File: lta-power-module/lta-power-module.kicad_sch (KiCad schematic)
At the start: 9 parts

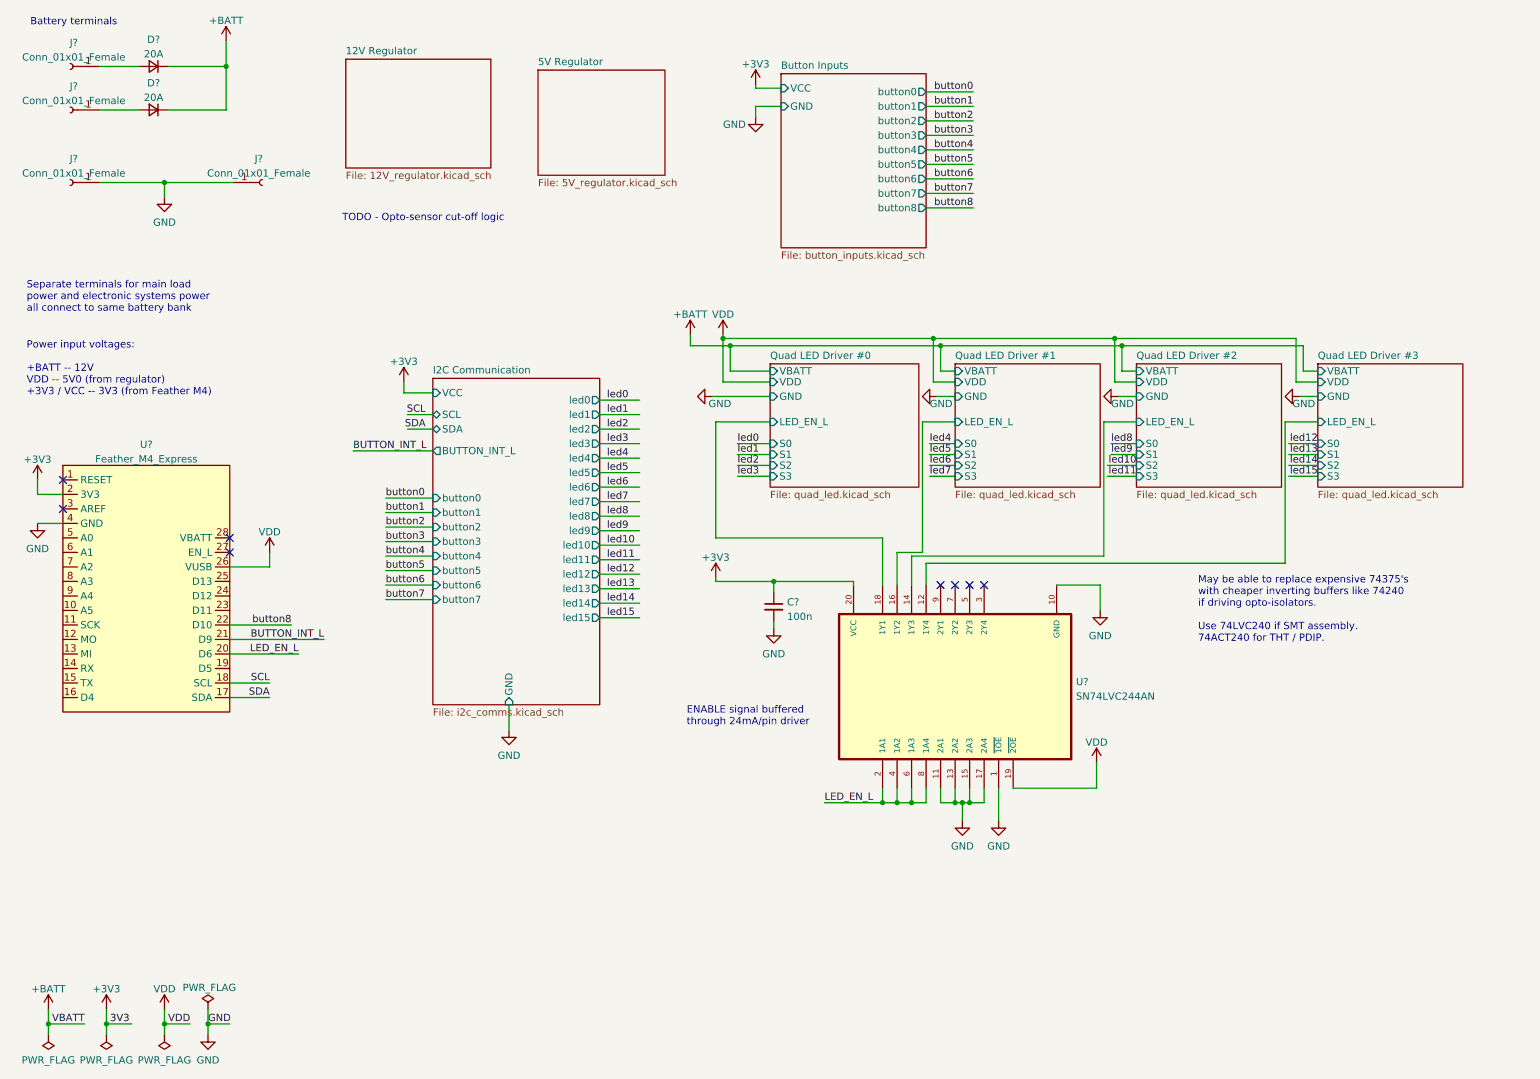
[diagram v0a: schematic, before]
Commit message: Power module main electrical schematic drawn, unannotated.
A logical schematic including flying wire connections between off-board
modules is sketched in the associated pptx file.
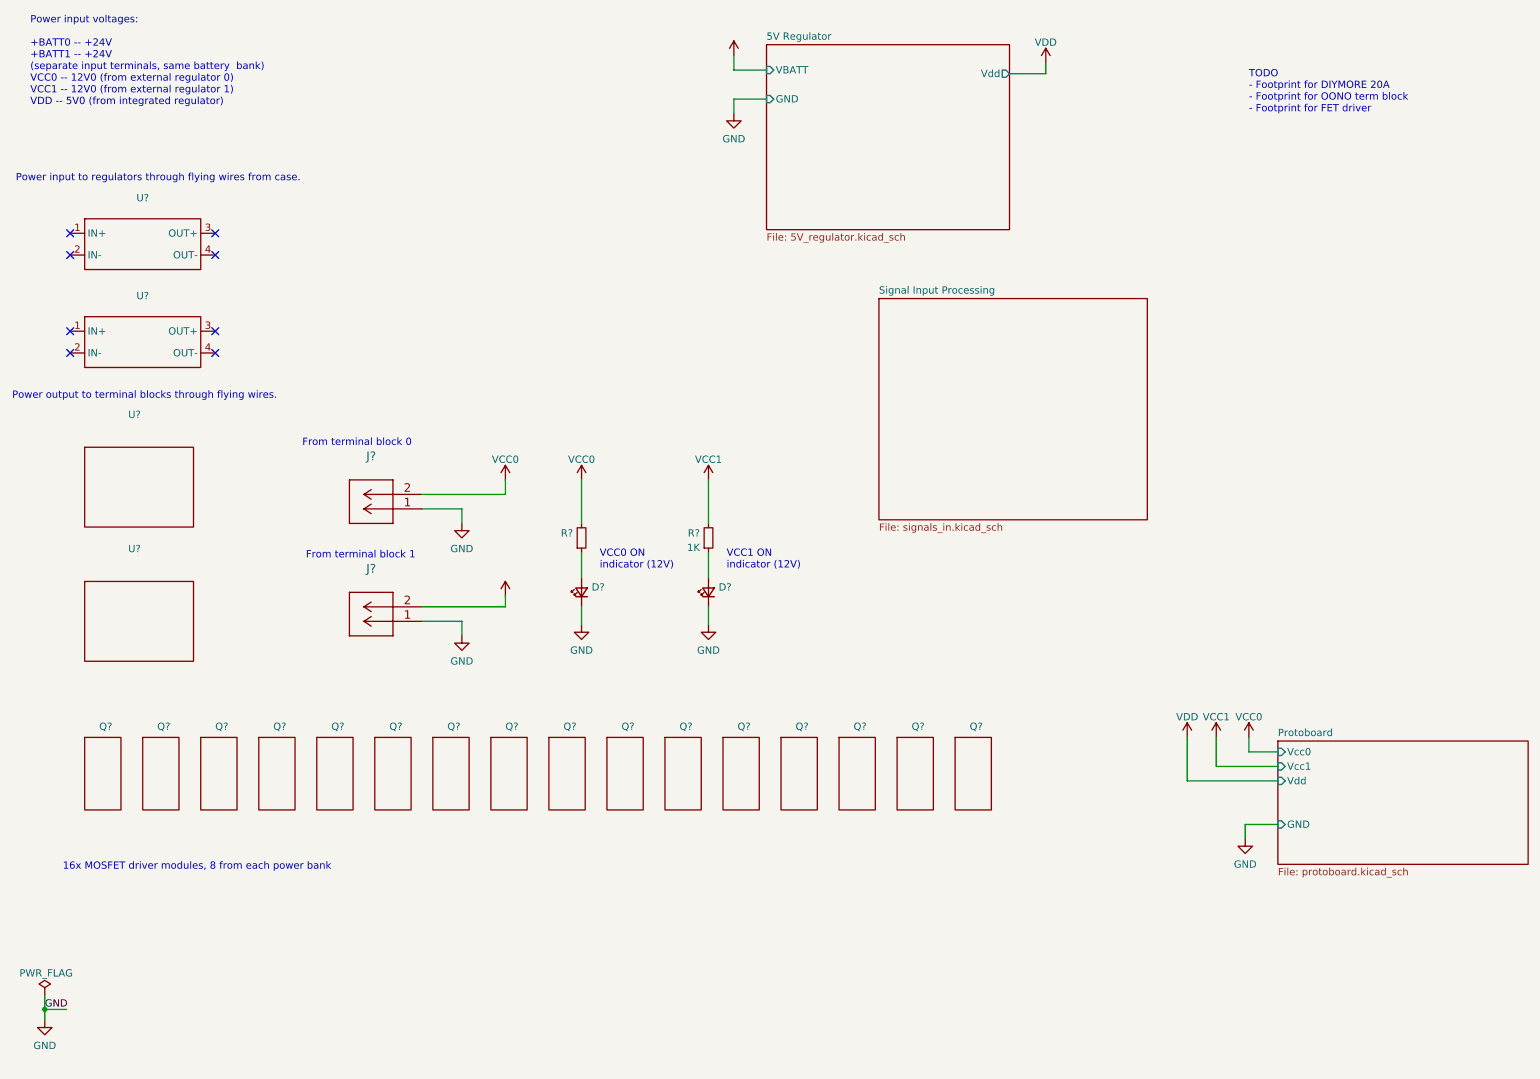
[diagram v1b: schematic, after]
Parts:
- removed C?: 100n, symbol Device:C_Small
- removed D? (x2): 20A, symbol Device:D_Small
- removed J? (x4): Conn_01x01_Female, symbol Connector:Conn_01x01_Female
- removed U?: SN74LVC244AN, Aaron_TI_Parts:TI_N_R-PDIP-T20, symbol Aaron-TI-Buffers:SN74LVC244AN
- removed U?: Feather_M4_Express, aaron-imported-parts:Arduino_Feather_M4_Express_PinHeaders, symbol Aaron-Arduino:Feather_M4_Express
- added D? (x2): (no value), symbol Device:LED_Small
- added J? (x2): (no value), symbol Aaron-Connectors:Molex-MicroLatch-53253-0270
- added Q? (x16): (no value), symbol lta-power-syms:Dual_MOSFET_Switch_Module
- added R?: (no value), symbol Device:R_Small
- added R?: 1K, symbol Device:R_Small
- added U? (x2): (no value), symbol lta-power-syms:OONO_16A_12pos_Terminal_Block
- added U? (x2): (no value), symbol lta-power-syms:DIYMORE_20A_Step_Down
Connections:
- net GND: now also D?.1 (K), D?.1 (K), J?.1, J?.1
- new net: D?.2 (A), R?.1 (x2)
- new net VCC0: J?.2, R?.2
- new net VCC1: J?.2, R?.2
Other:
- removed sheet 12V Regulator
- removed sheet Button Inputs
- removed sheet I2C Communication
- removed sheet Quad LED Driver #0
- removed sheet Quad LED Driver #1
- removed sheet Quad LED Driver #2
- removed sheet Quad LED Driver #3
- added sheet Protoboard (protoboard.kicad_sch)
- added sheet Signal Input Processing (signals_in.kicad_sch)
- sheet 5V Regulator ports: added GND, VBATT, Vdd; removed none
- note added: "16x MOSFET driver modules, 8 from each power bank"
- note added: "From terminal block 0"
- note added: "From terminal block 1"
- note added: "Power input to regulators through flying wires from case."
- note added: "Power input voltages: +BATT0 -- +24V +BATT1 -- +24V (separate input terminals, same battery bank) VCC0 -- 12V0 (from external regulator 0) VCC1 -- 12V0 (from external regulator 1) VDD -- 5V0 (from integrated regulator)"
- note added: "Power output to terminal blocks through flying wires."
- note added: "TODO - Footprint for DIYMORE 20A - Footprint for OONO term block - Footprint for FET driver"
- note added: "VCC0 ON indicator (12V)"
- note added: "VCC1 ON indicator (12V)"
- note removed: "Battery terminals"
- note removed: "ENABLE signal buffered through 24mA/pin driver"
- note removed: "May be able to replace expensive 74375's with cheaper inverting buffers like 74240 if driving opto-isolators. Use 74LVC240 if SMT assembly. 74ACT240 for THT / PDIP."
- note removed: "Power input voltages: +BATT -- 12V VDD -- 5V0 (from regulator) +3V3 / VCC -- 3V3 (from Feather M4)"
- note removed: "Separate terminals for main load power and electronic systems power all connect to same battery bank"
- note removed: "TODO - Opto-sensor cut-off logic"

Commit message: Small sheet cleanup.
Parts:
- added TP? (x3): TestPoint_Flag, Aaron_THT:TestPoint_THTPad_1.0x1.0mm_Drill0.3mm, symbol Connector:TestPoint_Flag
- R?: value 1K -> (none)
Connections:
- net GND: now also TP?.1
- net VCC0: now also TP?.1
- net VCC1: now also TP?.1
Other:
- sheet Signal Input Processing ports: added GND, Vcc0, Vdd; removed none
- note added: "${REV_DATE}"
- note added: "${REV}"
- note added: "YOU DON'T HAVE TO LIKE ALL THE ART!"
- note added: "YOU DON'T HAVE TO LIKE ALL THE ART! Main Power Module"

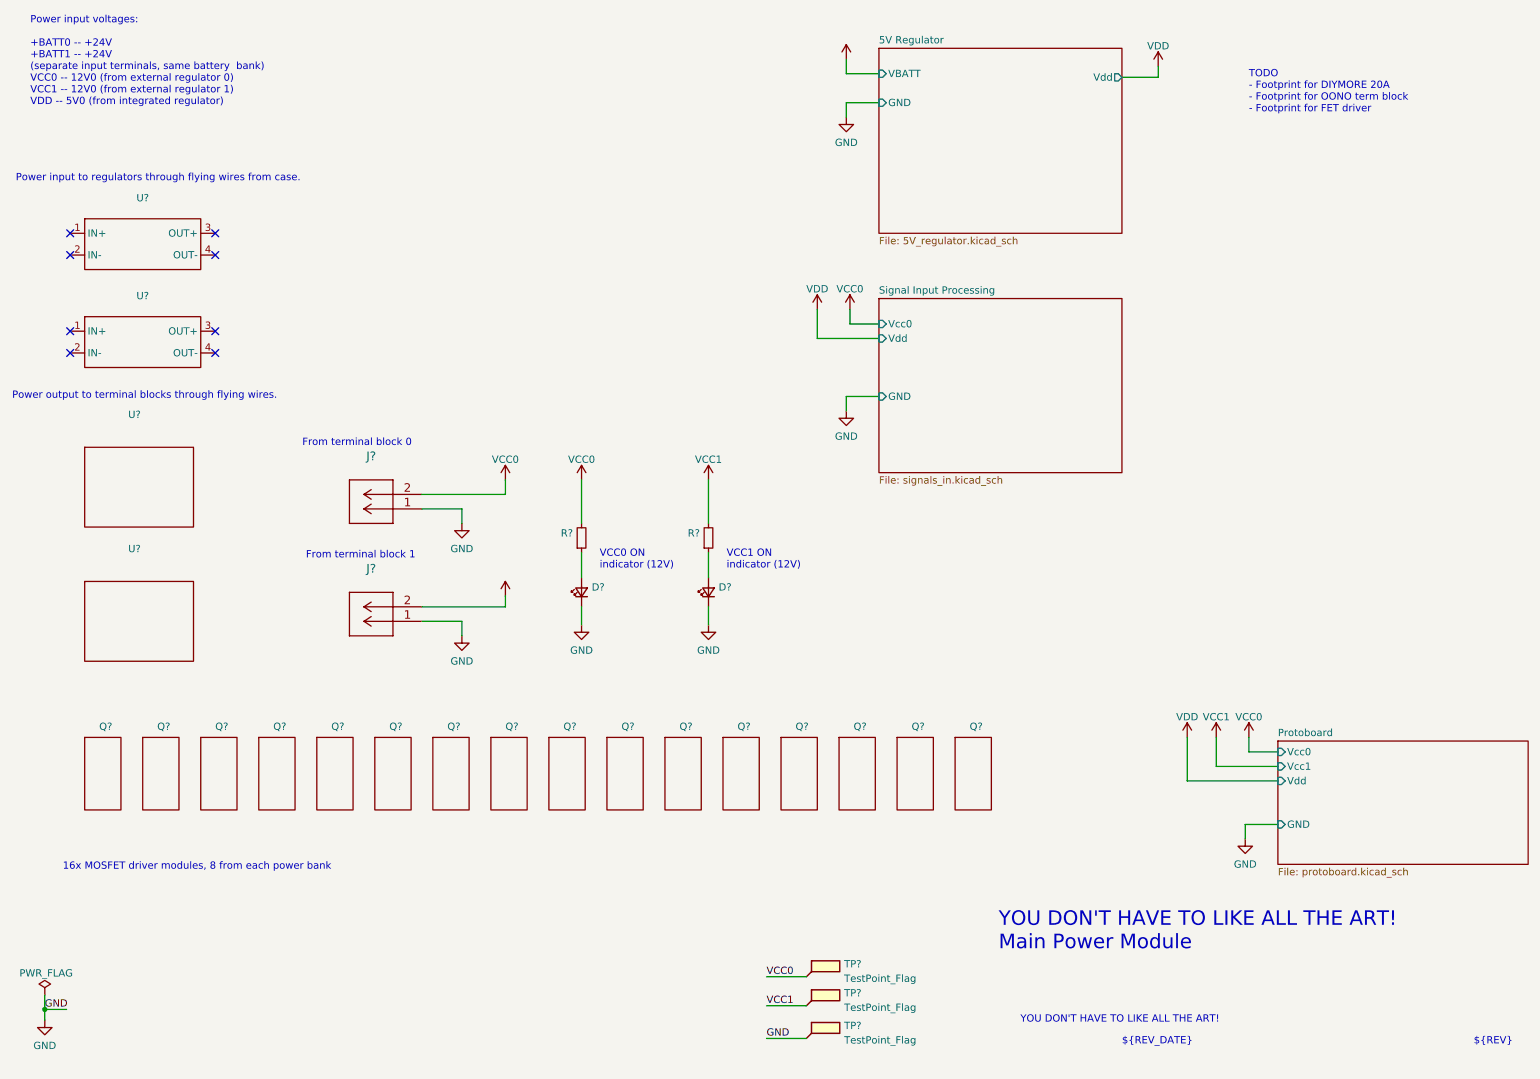
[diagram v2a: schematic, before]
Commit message: Add custom footprints for 12V regulator and power distribution bus.
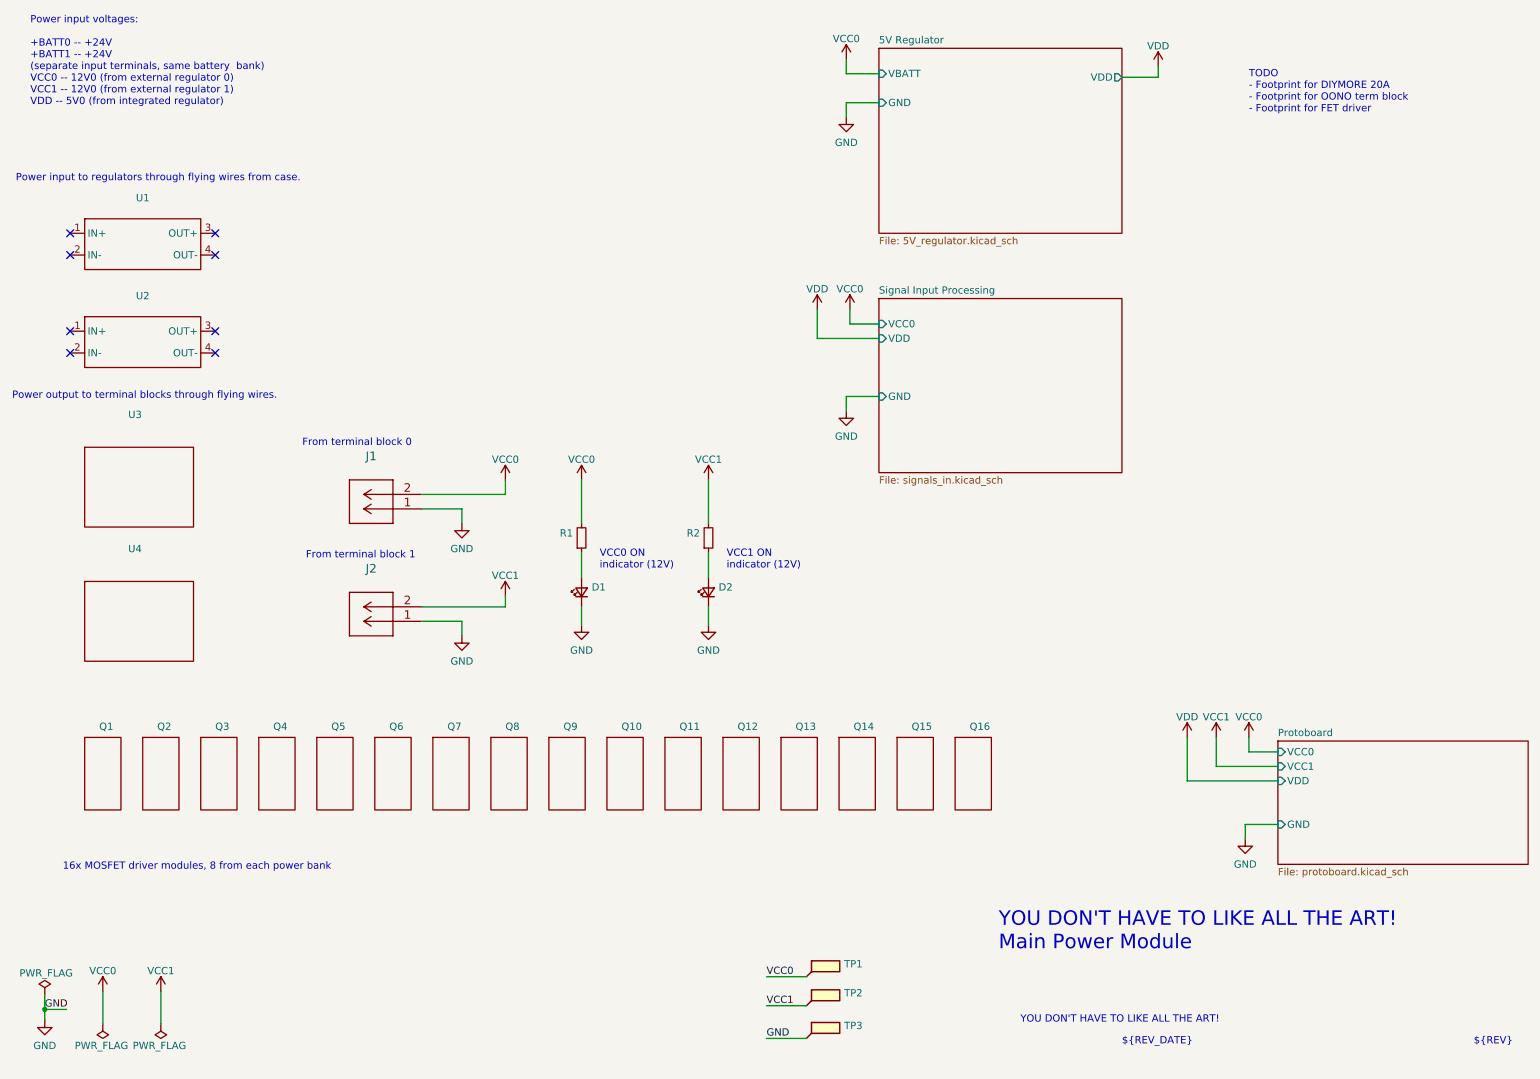
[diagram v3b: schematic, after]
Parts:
- D1, D2: renamed from D?; Comment Vf=2.0V I_test=20mA red LED -> Vf=2.0V I_test=20mA red LED 5mm THT; MANUFACTURER (none) -> CreeLED; MPN (none) -> C5SMF-RJF-CT0W0BB1
- J1, J2: renamed from J?; MANUFACTURER (none) -> Molex; MPN (none) -> 532530270
- R1, R2: renamed from R?; Comment 330R 0603 resistor; +/-1%; 1/10W -> 1K THT resistor; +/-5%; 1/4W; MANUFACTURER (none) -> Stackpole; MPN (none) -> CF14JT1K00
- TP1, TP2, TP3: renamed from TP?; value TestPoint_Flag -> (none); footprint Aaron_THT:TestPoint_THTPad_1.0x1.0mm_Drill0.3mm -> (none)
- gave numbers to parts that had none: 20
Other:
- sheet 5V Regulator ports: added VDD; removed Vdd
- sheet Protoboard ports: added VCC0, VCC1, VDD; removed Vcc0, Vcc1, Vdd
- sheet Signal Input Processing ports: added VCC0, VDD; removed Vcc0, Vdd
